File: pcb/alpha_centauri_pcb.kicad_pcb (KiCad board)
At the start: 2 copper layers, 280.7 x 98.8 mm, 208 parts, among them J1 USB_C_Receptacle_USB2.0_16P, J2 USB_C_Receptacle_USB2.0_16P, J3 USB_C_Receptacle_USB2.0_16P, J4 USB_C_Receptacle_USB2.0_16P, M1 Motor 2 +, M2 Motor 2 -, M3 Motor 1 -, M4 Motor 1 +, M5 Motor 1 +, M6 Motor 1 -, M7 Motor 2 +, M8 Motor 2 -, Q1 AO3400A, Q2 AO3400A, SW1 BOOTSEL, SW2 RESET, SW3 RESET, SW4 BOOTSEL, U1 W25Q128JVS, U2 RP2040, U3 AMS1117-3.3, U4 AMS1117-3.3, U5 RP2040, U6 W25Q128JVS, Y1 ABM8-272-T3, Y2 ABM8-272-T3

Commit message: Initial PCB v1.1.0 updates, including 4-layer restructure
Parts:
- added C35: 1u, Capacitor_SMD:C_0603_1608Metric, B.Cu at (360.8, 65.0)
- added C36: 1u, Capacitor_SMD:C_0603_1608Metric, B.Cu at (362.2, 65.0)
- added C37: 1u, Capacitor_SMD:C_0603_1608Metric, B.Cu at (121.2, 66.2)
- added C38: 1u, Capacitor_SMD:C_0603_1608Metric, B.Cu at (121.2, 67.8)
- added D83: GG0402052R542P, GG0402052R542P:DIONC1006X55N, B.Cu at (362.7, 60.9)
- added D84: GG0402052R542P, GG0402052R542P:DIONC1006X55N, B.Cu at (362.7, 58.5)
- added D85: GG0402052R542P, GG0402052R542P:DIONC1006X55N, B.Cu at (103.7, 57.6)
- added D86: GG0402052R542P, GG0402052R542P:DIONC1006X55N, B.Cu at (103.7, 56.4)
- added D87: GG0402052R542P, GG0402052R542P:DIONC1006X55N, B.Cu at (380.2, 58.0)
- added D88: GG0402052R542P, GG0402052R542P:DIONC1006X55N, B.Cu at (137.2, 63.5)
- added D89: GG0402052R542P, GG0402052R542P:DIONC1006X55N, B.Cu at (137.2, 65.8)
- added D91: GG0402052R542P, GG0402052R542P:DIONC1006X55N, B.Cu at (380.2, 60.5)
- added H11: Mounting_Hole, MountingHole:MountingHole_4.3mm_M4, F.Cu at (286.7, 53.1)
- added H12: Mounting_Hole, MountingHole:MountingHole_4.3mm_M4, F.Cu at (197.7, 56.1)
- added S41: SSAG230400, SSAG230400:SSAG230400, B.Cu at (214.1, 57.8)
- added S42: SSAG230400, SSAG230400:SSAG230400, B.Cu at (269.4, 59.8)
- SW1, SW2, SW3, SW4: footprint Button_Switch_SMD:SW_SPST_EVQP0 -> EVQ-P9P02W:EVQ-P9P02W
- U1, U6: footprint Package_SO:SOIC-8_5.23x5.23mm_P1.27mm -> W25Q128JVSIQ:SOIC127P790X216-8N
- moved R4 21.4 mm to (142.8, 68.0), turned to 0 degrees
- moved R5 20.5 mm to (142.8, 69.6), turned to 0 degrees
- moved D10 7.22 mm to (208.2, 56.5), turned to 0 degrees
- moved C15 6.67 mm to (195.2, 60.5), turned to 90 degrees
- moved D13 6.50 mm to (122.3, 58.0)
- moved C10 4.92 mm to (140.8, 85.7)
- moved C11 4.92 mm to (139.2, 85.7)
- moved SW3 4.49 mm to (286.0, 60.0)
- moved C20 3.74 mm to (289.5, 59.5), turned to -90 degrees
- moved SW2 3.66 mm to (198.2, 62.5), turned to -90 degrees
- moved H2 2.00 mm to (118.2, 50.8)
- moved R13 1.86 mm to (347.6, 59.1)
- moved J1 1.58 mm to (107.3, 49.7)
- moved J4 1.57 mm to (376.2, 49.7)
- moved H10 1.46 mm to (364.2, 50.5)
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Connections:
- M1 pad 1: 5v L -> Net-(S41-NO_1)
- M4 pad 1: 5v L -> Net-(S41-NO_1)
- M5 pad 1: 5v R -> Net-(S42-NO_1)
- M7 pad 1: 5v R -> Net-(S42-NO_1)
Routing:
- net 5v R: track 480.2 -> 40.8 mm, vias 29 -> 31
- net 5v L: track 478.3 -> 42.7 mm, vias 27 -> 30
- net Net-(S42-NO_1): track 0.00 -> 101.0 mm, vias 0 -> 4
- net Net-(S41-NO_1): track 0.00 -> 89.0 mm, vias 0 -> 2
- net 3v3 L: track 151.3 -> 66.0 mm, vias 13 -> 17
- net GND L: track 11.3 -> 80.1 mm, vias 189 -> 64
- net GND R: track 30.3 -> 95.8 mm, vias 280 -> 58
- net 3v3 R: track 139.0 -> 73.5 mm, vias 12 -> 14
- net D28 R: track 138.0 -> 84.6 mm, vias 14 -> 6
- net D29 R: track 141.5 -> 98.1 mm, vias 16 -> 7
- net QSPI_SS R: track 95.8 -> 127.4 mm, vias 8 -> 4
- net D0 R: track 117.9 -> 88.6 mm, vias 10 -> 8
- net L DN: track 25.4 -> 52.3 mm
- net L DP: track 25.1 -> 48.6 mm, vias 2 -> 4
- net Net-(U2-RUN): track 82.7 -> 105.7 mm
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- added copper zone on In2.Cu, net 3v3 L
- added copper zone on In2.Cu, net 3v3 R
- added copper zone on In2.Cu, net 5v L
- added copper zone on In2.Cu, net 5v R
- added copper zone on In1.Cu, net GND L
- added copper zone on In1.Cu, net GND R
- removed copper zone on B.Cu, net GND L
- removed copper zone on F.Cu, net GND L
- removed copper zone on B.Cu, net GND R
- removed copper zone on F.Cu, net GND R
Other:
- board size 280.7 x 98.8 mm -> 279.5 x 97 mm
- copper layers 2 -> 4
- board text added: "Alpha Centauri v1.1 github.com/jacob-w-gable/alpha_centauri"
- board text removed: "Alpha Centauri v1.0 github.com/jacob-w-gable/alpha_centauri"

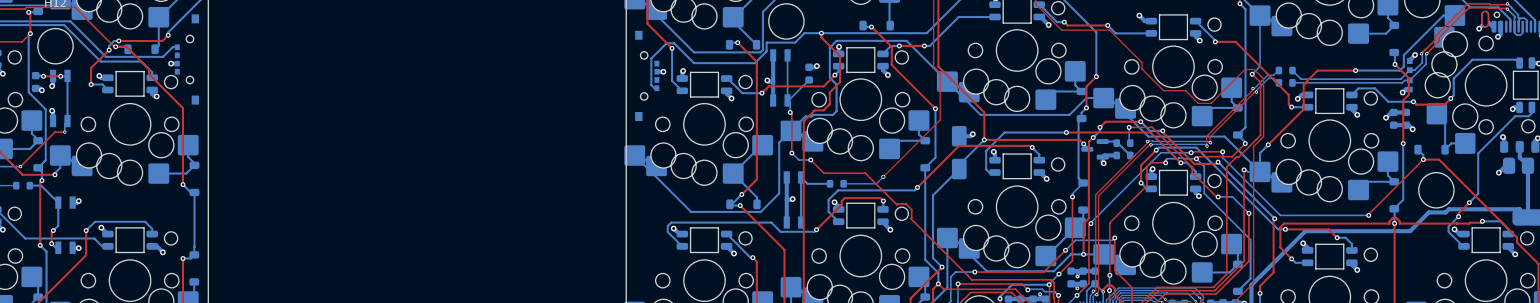
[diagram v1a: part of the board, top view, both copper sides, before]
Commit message: Include components as a path in the repository
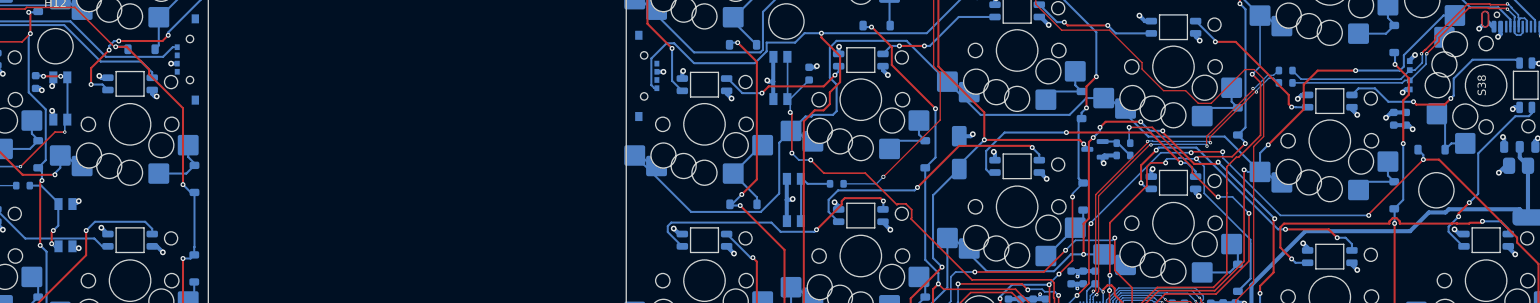
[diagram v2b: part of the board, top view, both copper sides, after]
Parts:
- S1, S10, S11, S12, S13, S14, S15, S16, S17, S18, S19, S2, S20, S21, S22, S23, S24, S25, S26, S27, S28, S29, S3, S30, S31, S32, S33, S34, S35, S36, S37, S39, S4, S40, S5, S6, S7, S9: footprint JacobGable:MX_Choc_Hotswap_Hybrid -> AlphaCentauri:MX_Choc_Hotswap_Hybrid
- S38, S8: footprint JacobGable:MX_Choc_Hotswap_Hybrid_1.5u -> AlphaCentauri:MX_Choc_Hotswap_Hybrid_1.5u
- SW1, SW2, SW3, SW4: footprint EVQ-P9P02W:EVQ-P9P02W -> EVQ-P9P02W:EVQP2202M
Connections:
- J1 pad SH: GND L -> (no net)
- J2 pad SH: GND L -> (no net)
- J3 pad SH: GND R -> (no net)
- J4 pad SH: GND R -> (no net)
